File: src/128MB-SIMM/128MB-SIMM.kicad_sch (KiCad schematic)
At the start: 30 parts, among them J2 Conn_02x03_Odd_Even, J4 128MB, U1 LM1117-3.3, U2 74LVC4245A, U3 74LVC4245A, U4 S29GL01GS, U5 74LVC245A, U6 74LVC245A, U7 74LVC245A, U8 74LVC245A, U9 74LS148

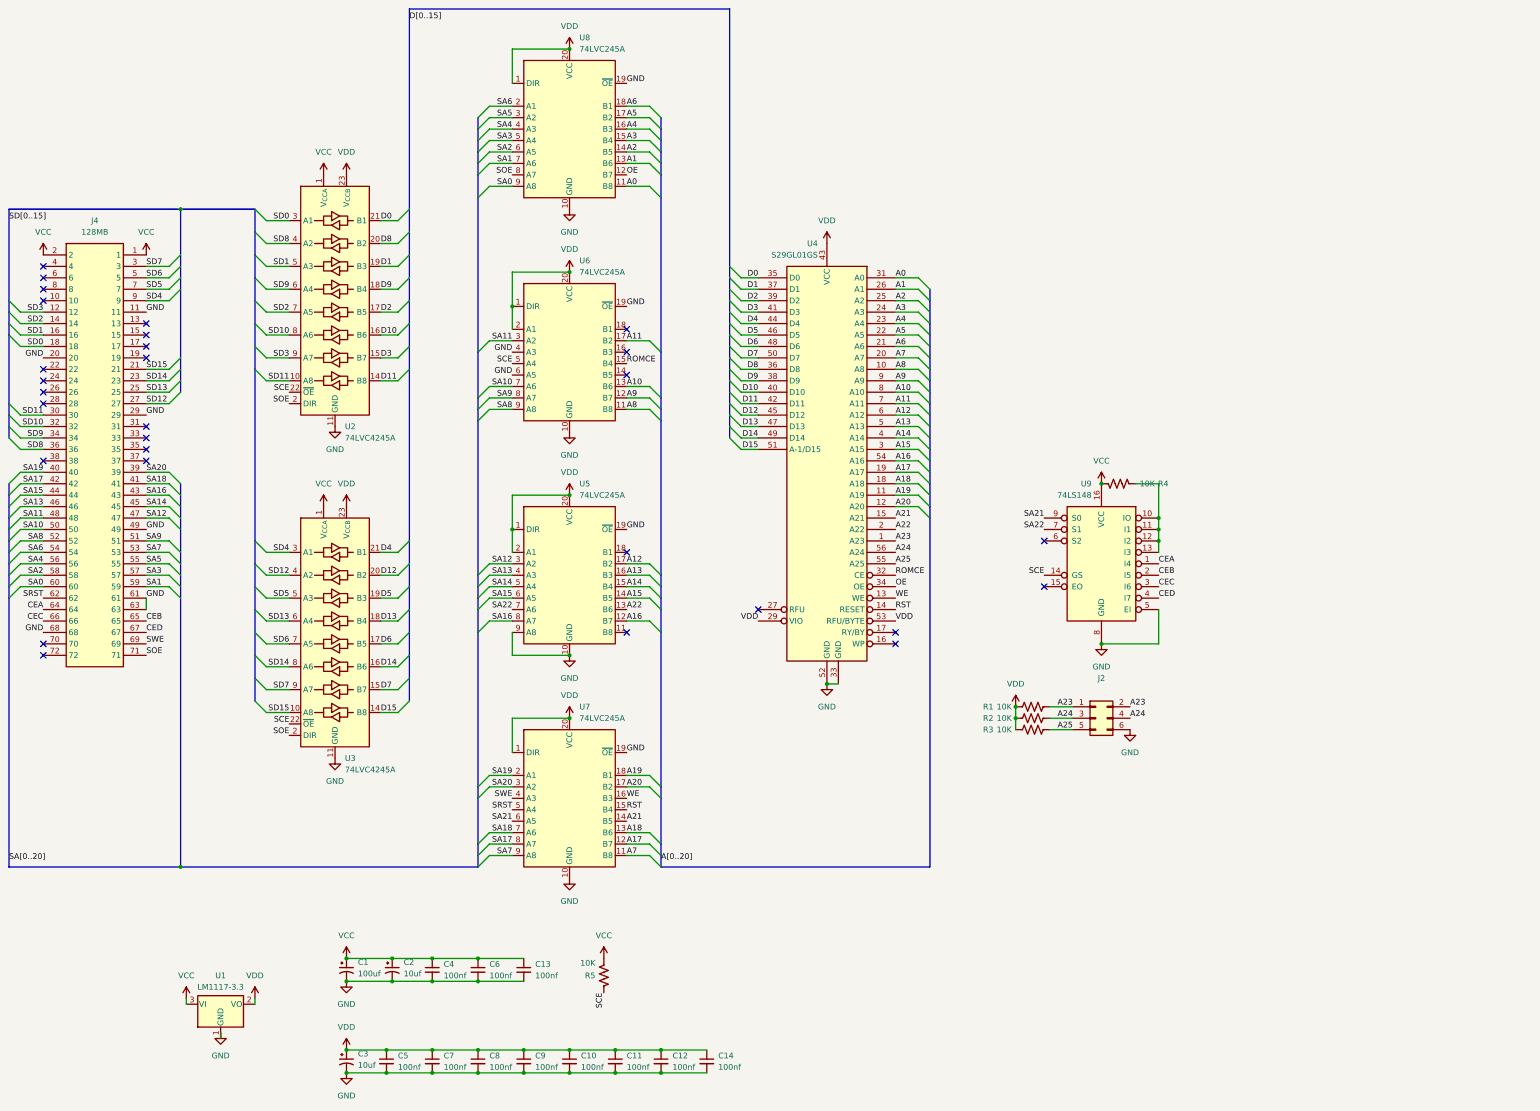
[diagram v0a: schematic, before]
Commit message: update source files changed LS41 by LVC00 and LVC08
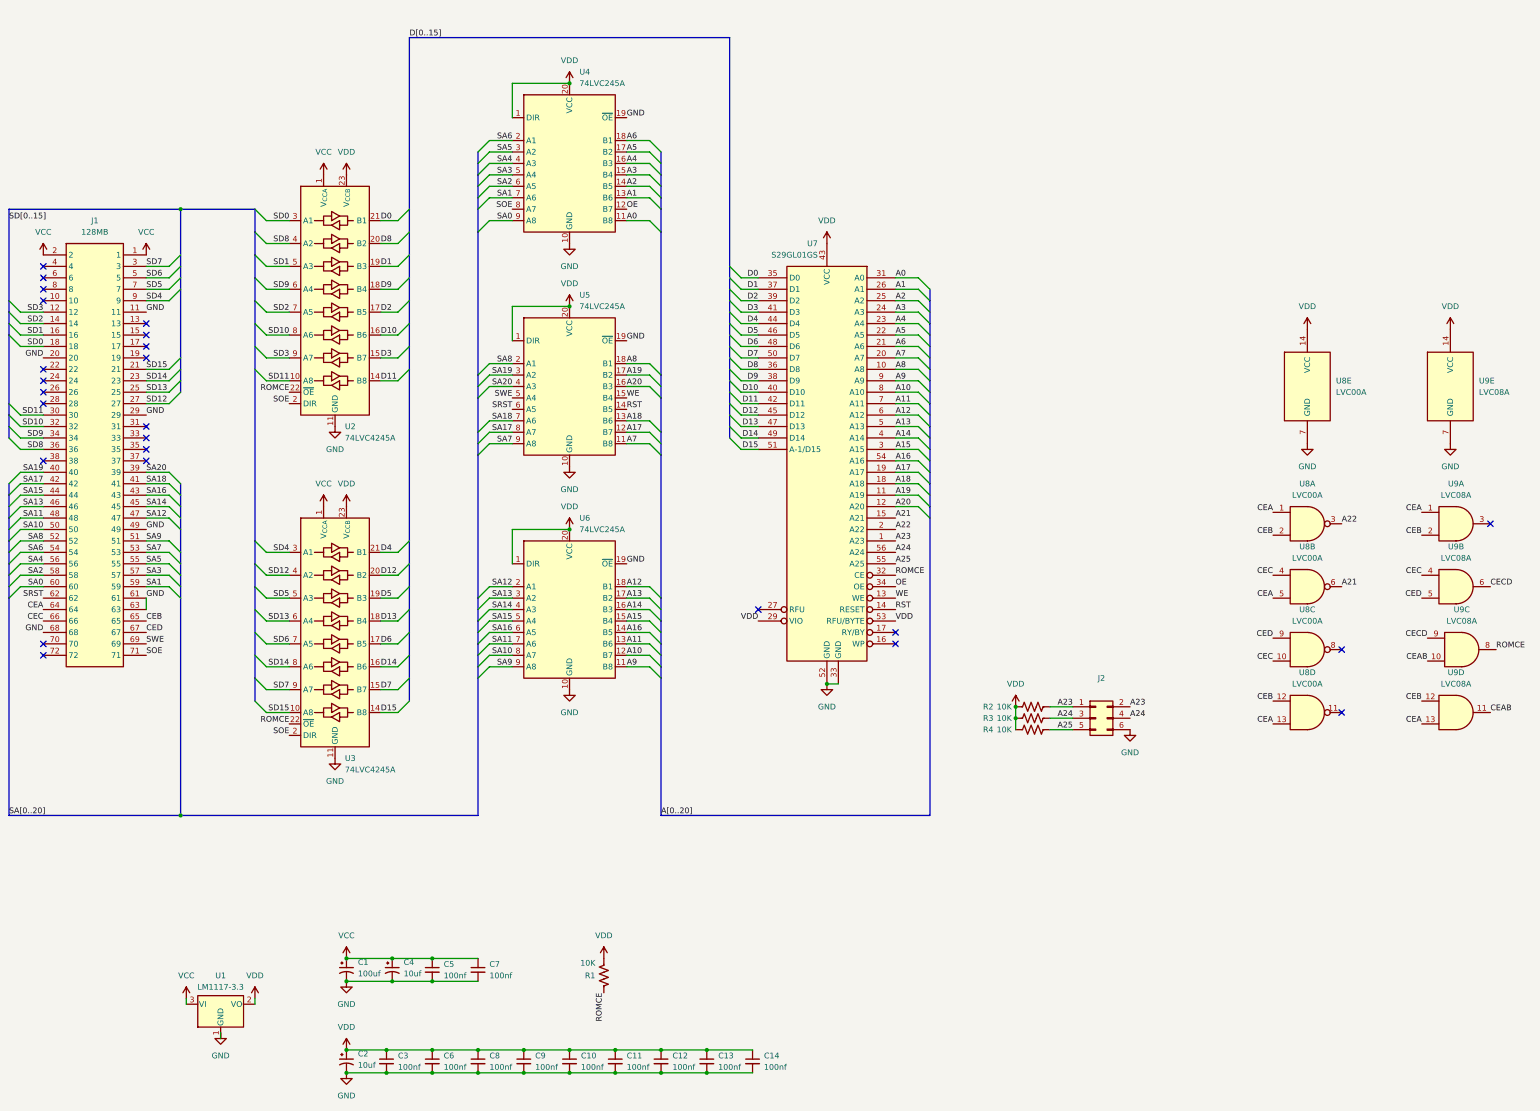
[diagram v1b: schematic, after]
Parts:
- removed C12: 100nf, Capacitor_SMD:C_0603_1608Metric, symbol Device:C_Small
- removed R4: 10K, Resistor_SMD:R_0603_1608Metric, symbol Device:R_US
- removed U7: 74LVC245A, Package_SO:TSSOP-20_4.4x6.5mm_P0.65mm, symbol Logic_LevelTranslator:SN74LVC245APW
- removed U9: 74LS148, Package_SO:SOIC-16_3.9x9.9mm_P1.27mm, symbol 74xx:74LS148
- added C14: 100nf, Capacitor_SMD:C_0603_1608Metric, symbol Device:C_Small
- added U8: LVC00A, Package_SO:TSSOP-14_4.4x5mm_P0.65mm, symbol 74xx:74LS00
- added U9: LVC08A, Package_SO:TSSOP-14_4.4x5mm_P0.65mm, symbol 74xx:74LS08
- J1: renamed from J4; now left out of the parts list
- renumbered C13 to C12, C14 to C13, C3 to C2, C5 to C3, C2 to C4, C4 to C5, C7 to C6, C6 to C7, R5 to R1, R1 to R2, R2 to R3, R3 to R4, U8 to U4, U6 to U5, U5 to U6, U4 to U7
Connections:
- net SA22 is gone; now on net SA11: U6.7 (A6)
- net A10: now also U6.12 (B7); no longer U5.13 (B6)
- net A11: now also U6.13 (B6); no longer U5.17 (B2)
- net A12: now also U6.18 (B1); no longer U6.17 (B2)
- net A13: now also U6.17 (B2); no longer U6.16 (B3)
- net A14: now also U6.16 (B3); no longer U6.15 (B4)
- net A15: now also U6.15 (B4); no longer U6.14 (B5)
- net A16: now also U6.14 (B5); no longer U6.12 (B7)
- net A17: now also U5.12 (B7)
- net A18: now also U5.13 (B6)
- net A19: now also U5.17 (B2)
- net A20: now also U5.16 (B3)
- net A21: now also U8.6
- net A22: now also U8.3; no longer U6.13 (B6)
- net A7: now also U5.11 (B8)
- net A8: now also U5.18 (B1); no longer U5.11 (B8)
- net A9: now also U6.11 (B8); no longer U5.12 (B7)
- net CEA: now also U8.1, U8.13, U8.5, U9.1, U9.13
- net CEB: now also U8.12, U8.2, U9.12, U9.2
- net CEC: now also U8.10, U8.4, U9.4
- net CED: now also U8.9, U9.5
- net GND: now also C14.2, U8.7 (GND), U9.7 (GND); no longer U5.4 (A3), U5.6 (A5), U6.9 (A8)
- net ROMCE: now also R1.1, U2.22 (~{OE}), U3.22 (~{OE}), U9.8; no longer U5.15 (B4)
- net RST: now also U5.14 (B5)
- net SA10: now also U6.8 (A7); no longer U5.7 (A6)
- net SA11: no longer U5.3 (A2)
- net SA12: now also U6.2 (A1); no longer U6.3 (A2)
- net SA13: now also U6.3 (A2); no longer U6.4 (A3)
- net SA14: now also U6.4 (A3); no longer U6.5 (A4)
- net SA15: now also U6.5 (A4); no longer U6.6 (A5)
- net SA16: now also U6.6 (A5); no longer U6.8 (A7)
- net SA17: now also U5.8 (A7)
- net SA18: now also U5.7 (A6)
- net SA19: now also U5.3 (A2)
- net SA20: now also U5.4 (A3)
- net SA7: now also U5.9 (A8)
- net SA8: now also U5.2 (A1); no longer U5.9 (A8)
- net SA9: now also U6.9 (A8); no longer U5.8 (A7)
- net SRST: now also U5.6 (A5)
- net SWE: now also U5.5 (A4)
- net VCC: no longer C12.1, R1.2
- net VDD: now also C12.1, R1.2, C14.1, U8.14 (VCC), U9.14 (VCC); no longer U5.2 (A1), U6.2 (A1)
- net WE: now also U5.15 (B4)
- removed net SCE: R1.1, U2.22 (~{OE}), U3.22 (~{OE}), U5.5 (A4)
- new net CEAB: U9.10, U9.11
- new net CECD: U9.6, U9.9
- no-connect marks 29 -> 25
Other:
- moved on the sheet: C12, U4, U5, U6
